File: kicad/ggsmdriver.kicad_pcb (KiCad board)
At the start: 4 copper layers, 55 x 45 mm, 69 parts, among them J1 DC-005, J2 VIN 9-24V, J3 MOTOR A1 A2 B1 B2, J4 EXP, J5 USB-C, SW1 BOOT, SW2 RESET, U1 STM32G0B1CBT6, U2 TMC2209-LA, U3 TPS54202DDCR, U4 XC6206P332MR, U5 USBLC6-2SC6

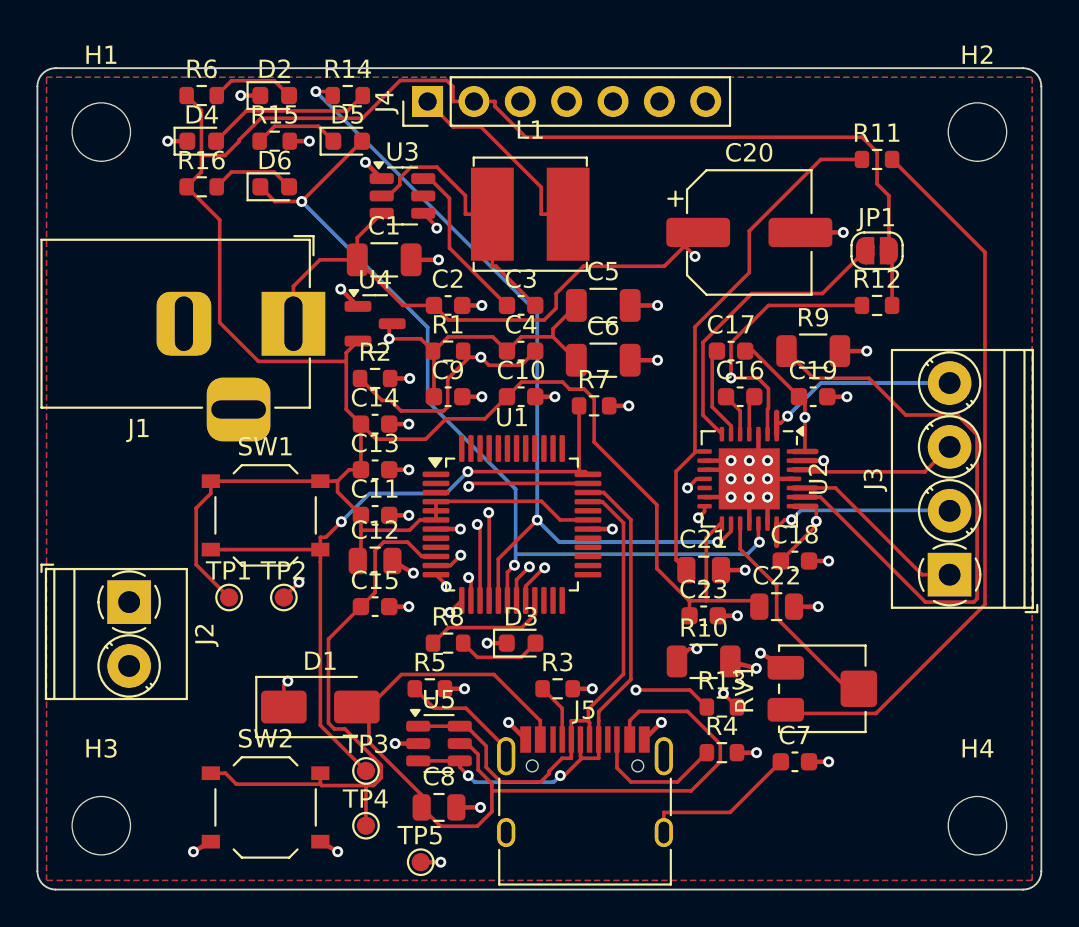
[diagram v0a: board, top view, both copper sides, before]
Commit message: PCB: hand-laid TMC2209 power stage, no VREF trimmer, real track widths
Motor outputs run 1 mm wide straight to J3 next to the chip (J3 now A2 A1 B1 B2),
sense resistors and VS vias sit at the driver pins, VS caps join through a new
In2.Cu VIN plane, as on the Adafruit breakout. VREF goes to GND since current is
always set over UART. Netclass widths now reach the router. Fully routed, no DRC
errors; fab files regenerated.

Co-Authored-By: Claude Opus 5.5 (1M context) <noreply@anthropic.com>
Claude-Session: https://claude.ai/code/session_01VFhb1Qv7mkaGrgvtw2CS4q
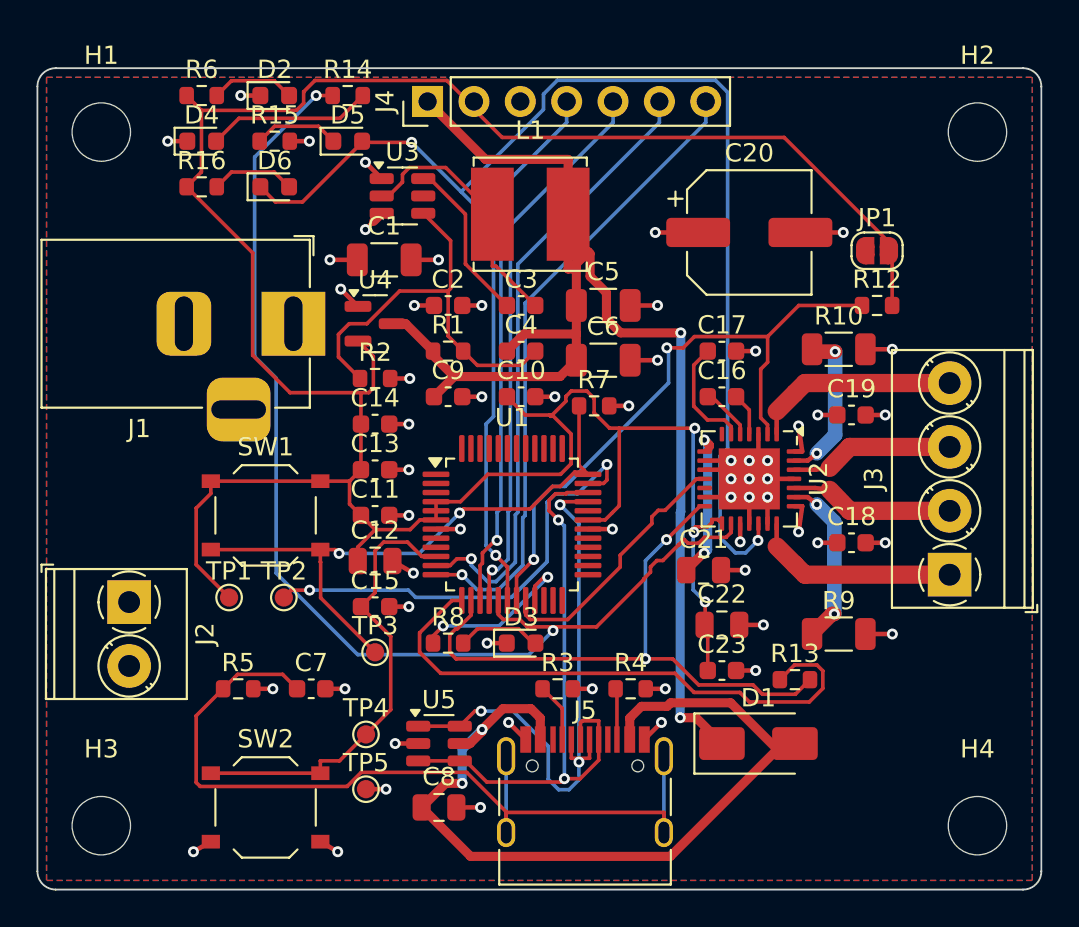
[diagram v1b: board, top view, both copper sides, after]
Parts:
- removed R11: 33k, Resistor_SMD:R_0603_1608Metric
- removed RV1: 10k current, Potentiometer_SMD:Potentiometer_Bourns_3314J_Vertical
- J3: value MOTOR A1 A2 B1 B2 -> MOTOR A2 A1 B1 B2
- moved C7 26.8 mm to (115.0, 134.0)
- moved D1 24.1 mm to (139.5, 137.0)
- moved R10 18.6 mm to (143.9, 115.4)
- moved R9 15.6 mm to (143.9, 131.0)
- moved R5 10.5 mm to (111.0, 134.0)
- moved TP3 6.52 mm to (118.5, 132.0)
- moved R4 6.10 mm to (132.5, 134.0)
- moved TP4 5.00 mm to (118.0, 136.5)
- moved TP5 5.00 mm to (118.0, 139.5)
- moved R13 4.27 mm to (141.5, 133.5)
- moved C18 3.26 mm to (144.6, 126.0)
- moved C22 3.16 mm to (137.5, 130.5)
- moved C23 3.16 mm to (137.5, 133.0)
- moved C19 2.33 mm to (144.6, 119.0)
- moved C16 1.00 mm to (137.5, 118.0)
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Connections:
- J3 pad 1: MOT_A1 -> MOT_A2
- J3 pad 2: MOT_A2 -> MOT_A1
- U2 pad 17: TMC_VREF -> GND
- U2 pad 7: TMC_SPREAD -> (no net)
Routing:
- net VIN: track 83.2 -> 13.8 mm, vias 3 -> 9
- net TMC_POT: track 40.0 -> 0.00 mm
- net TMC_DIR: track 48.8 -> 83.8 mm
- net TMC_BRA: track 33.8 -> 9.46 mm, vias 0 -> 2
- net TMC_5V: track 28.8 -> 8.59 mm, vias 0 -> 2
- net TMC_STEP: track 46.6 -> 63.5 mm, vias 3 -> 2
- net TMC_SPREAD: track 16.4 -> 0.00 mm
- net USB_SHIELD: track 32.4 -> 48.0 mm
- net TMC_TX: track 17.2 -> 31.4 mm, vias 2 -> 0
- net TMC_VREF: track 12.1 -> 0.00 mm
- net TMC_UART: track 25.4 -> 34.2 mm, vias 3 -> 2
- net TMC_BRB: track 16.2 -> 8.70 mm
- net BOOT0_SWCLK: track 39.7 -> 33.2 mm
- net +5V: track 65.2 -> 71.7 mm
- net NRST: track 31.5 -> 25.3 mm
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- added copper zone on In2.Cu, net VIN

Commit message: PCB round 2: no barrel jack, power terminal beside motor terminal, stocked parts
J1 removed; the VIN/GND terminal sits right below the motor terminal on the right
edge. TMC2209-LA-T (C2150710), RALEC 50 mOhm 1206 sense resistors (C154645), red
Basic / green LEDs replace out-of-stock parts. SPREAD pin reconnected (lost in the
previous edit). Fully routed, no DRC errors; fab files regenerated.

Co-Authored-By: Claude Opus 5.5 (1M context) <noreply@anthropic.com>
Claude-Session: https://claude.ai/code/session_01VFhb1Qv7mkaGrgvtw2CS4q
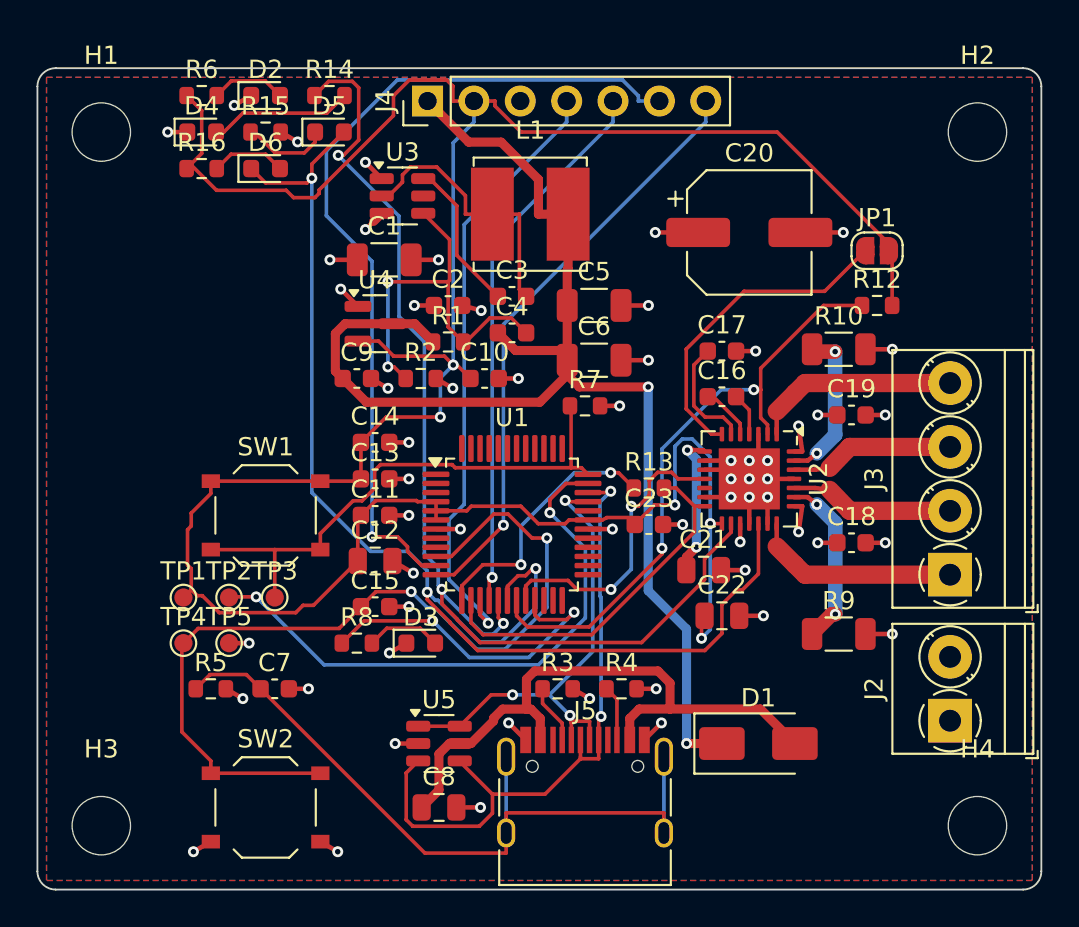
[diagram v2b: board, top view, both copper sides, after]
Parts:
- removed J1: DC-005, Connector_BarrelJack:BarrelJack_Horizontal
- D2: value PWR green -> PWR red
- D3: value STATUS blue -> STATUS green
- D4: value STEP yellow -> STEP red
- J2: value VIN 9-24V -> VIN 9-24V GND
- U2: value TMC2209-LA -> TMC2209-LA-T
- moved J2 45.4 mm to (150.0, 135.8), turned to 90 degrees
- moved R13 13.2 mm to (133.5, 123.0)
- moved TP4 11.2 mm to (108.0, 131.5)
- moved TP5 11.0 mm to (110.5, 131.5)
- moved C23 8.94 mm to (133.5, 125.0)
- moved TP3 6.26 mm to (113.0, 129.0)
- moved D3 5.50 mm to (121.0, 131.5)
- moved C9 5.10 mm to (117.5, 117.0)
- moved R8 5.00 mm to (117.5, 131.5)
- moved TP2 3.00 mm to (110.5, 129.0)
- moved R2 2.50 mm to (121.0, 117.0)
- moved TP1 2.50 mm to (108.0, 129.0)
- moved C10 2.24 mm to (124.5, 117.0)
- moved C7 2.00 mm to (113.0, 134.0)
- moved R5 1.50 mm to (109.5, 134.0)
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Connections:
- U2 pad 7: (no net) -> TMC_SPREAD
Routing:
- net NRST: track 25.3 -> 48.5 mm, vias 0 -> 2
- net TMC_SPREAD: track 0.00 -> 17.8 mm
- net TMC_TX: track 31.4 -> 14.4 mm, vias 0 -> 2
- net TMC_UART: track 34.2 -> 20.1 mm, vias 2 -> 0
- net VBUS: track 47.6 -> 34.0 mm, vias 2 -> 0
- net ENC_A: track 34.2 -> 47.0 mm
- net TMC_DIR: track 83.8 -> 71.4 mm
- net LED_STAT_R: track 9.71 -> 18.3 mm
- net SWDIO: track 24.9 -> 31.9 mm
- net USB_SHIELD: track 48.0 -> 41.7 mm
- net USB_DM: track 32.6 -> 26.4 mm
- net IO1: track 29.4 -> 33.6 mm
- net USB_DP: track 32.9 -> 36.2 mm
- net BOOT0_SWCLK: track 33.2 -> 29.9 mm, vias 2 -> 0
- net +3V3: track 149.8 -> 153.0 mm, vias 3 -> 5
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
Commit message: PCB: stocked 22 uF cap and three 2-pole terminals
C20 is now Lelon VES220M1HTR-0605 (C176676). The out-of-stock 4-pole motor terminal is
split into two KF350-3.5-2P blocks (J6 coil B, J3 coil A), so power and motor are three
identical 2P blocks along the right edge. Coil B tracks, R10 and C19 moved to make room.
Fully routed, no DRC errors; fab files regenerated.

Co-Authored-By: Claude Opus 5.5 (1M context) <noreply@anthropic.com>
Claude-Session: https://claude.ai/code/session_01VFhb1Qv7mkaGrgvtw2CS4q
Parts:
- added J6: MOTOR B1 B2, TerminalBlock_Phoenix:TerminalBlock_Phoenix_PT-1,5-2-3.5-H_1x02_P3.50mm_Horizontal, F.Cu at (150.0, 119.5)
- C20: footprint Capacitor_SMD:CP_Elec_6.3x5.9 -> Capacitor_SMD:CP_Elec_6.3x5.4
- J3: value MOTOR A2 A1 B1 B2 -> MOTOR A2 A1; footprint TerminalBlock_Phoenix:TerminalBlock_Phoenix_PT-1,5-4-3.5-H_1x04_P3.50mm_Horizontal -> TerminalBlock_Phoenix:TerminalBlock_Phoenix_PT-1,5-2-3.5-H_1x02_P3.50mm_Horizontal
- moved R10 2.48 mm to (142.0, 113.8)
- moved C19 1.25 mm to (144.6, 117.8)
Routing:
- net TMC_TX: track 14.4 -> 51.7 mm
- net BOOT0_SWCLK: track 29.9 -> 63.5 mm, vias 0 -> 2
- net TMC_EN: track 34.0 -> 58.7 mm, vias 2 -> 0
- net TMC_UART: track 20.1 -> 42.7 mm, vias 0 -> 2
- net NRST: track 48.5 -> 32.0 mm, vias 2 -> 0
- net USB_DM: track 26.4 -> 40.9 mm, vias 3 -> 2
- net ENC_A: track 47.0 -> 34.8 mm
- net TMC_DIR: track 71.4 -> 59.8 mm, vias 3 -> 4
- net SWDIO: track 31.9 -> 23.7 mm, vias 2 -> 0
- net +3V3: track 153.0 -> 144.9 mm
- net TMC_STEP: track 60.7 -> 68.2 mm, vias 3 -> 4
- net BUCK_FB: track 21.5 -> 15.9 mm, vias 2 -> 0
- net IO1: track 33.6 -> 36.7 mm
- net LED_STAT_R: track 18.3 -> 16.2 mm
- net TMC_BRB: track 8.70 -> 10.1 mm
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
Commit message: PCB: one 6-pole 2.54 mm terminal for power and motor
KF128-2.54-6P (C474924) replaces the three 3.5 mm 2-pole blocks, as on the Adafruit
breakout. Motor tracks re-laid to the 2.54 mm pins. Fully routed, no DRC errors; fab files
regenerated.

Co-Authored-By: Claude Opus 5.5 (1M context) <noreply@anthropic.com>
Claude-Session: https://claude.ai/code/session_01VFhb1Qv7mkaGrgvtw2CS4q
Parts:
- removed J2: VIN 9-24V GND, TerminalBlock_Phoenix:TerminalBlock_Phoenix_PT-1,5-2-3.5-H_1x02_P3.50mm_Horizontal
- removed J6: MOTOR B1 B2, TerminalBlock_Phoenix:TerminalBlock_Phoenix_PT-1,5-2-3.5-H_1x02_P3.50mm_Horizontal
- J3: value MOTOR A2 A1 -> VIN GND A2 A1 B1 B2; footprint TerminalBlock_Phoenix:TerminalBlock_Phoenix_PT-1,5-2-3.5-H_1x02_P3.50mm_Horizontal -> TerminalBlock_Phoenix:TerminalBlock_Phoenix_MPT-0,5-6-2.54_1x06_P2.54mm_Horizontal
- moved J3 3.90 mm to (151.4, 131.4)
- moved C18 2.40 mm to (144.6, 128.4)
- moved C19 1.15 mm to (144.6, 116.6)
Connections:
- J3 pad 1: MOT_A2 -> VIN
- J3 pad 2: MOT_A1 -> GND
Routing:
- net TMC_TX: track 51.7 -> 18.2 mm
- net BOOT0_SWCLK: track 63.5 -> 32.2 mm, vias 2 -> 0
- net SWDIO: track 23.7 -> 53.1 mm, vias 0 -> 2
- net TMC_UART: track 42.7 -> 21.8 mm
- net TMC_EN: track 58.7 -> 38.9 mm, vias 0 -> 2
- net VBUS: track 34.1 -> 53.4 mm
- net LED_STAT_R: track 16.2 -> 30.6 mm
- net USB_DM: track 40.9 -> 29.1 mm
- net +3V3: track 144.9 -> 136.6 mm, vias 5 -> 2
- net USB_DP: track 36.6 -> 44.2 mm
- net +5V: track 73.4 -> 77.2 mm, vias 3 -> 2
- net TMC_STEP: track 68.2 -> 64.7 mm, vias 4 -> 3
- net TMC_DIAG: track 16.4 -> 19.7 mm, vias 0 -> 2
- net TMC_DIR: track 59.8 -> 62.8 mm, vias 4 -> 3
- net IO1: track 36.7 -> 34.0 mm
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
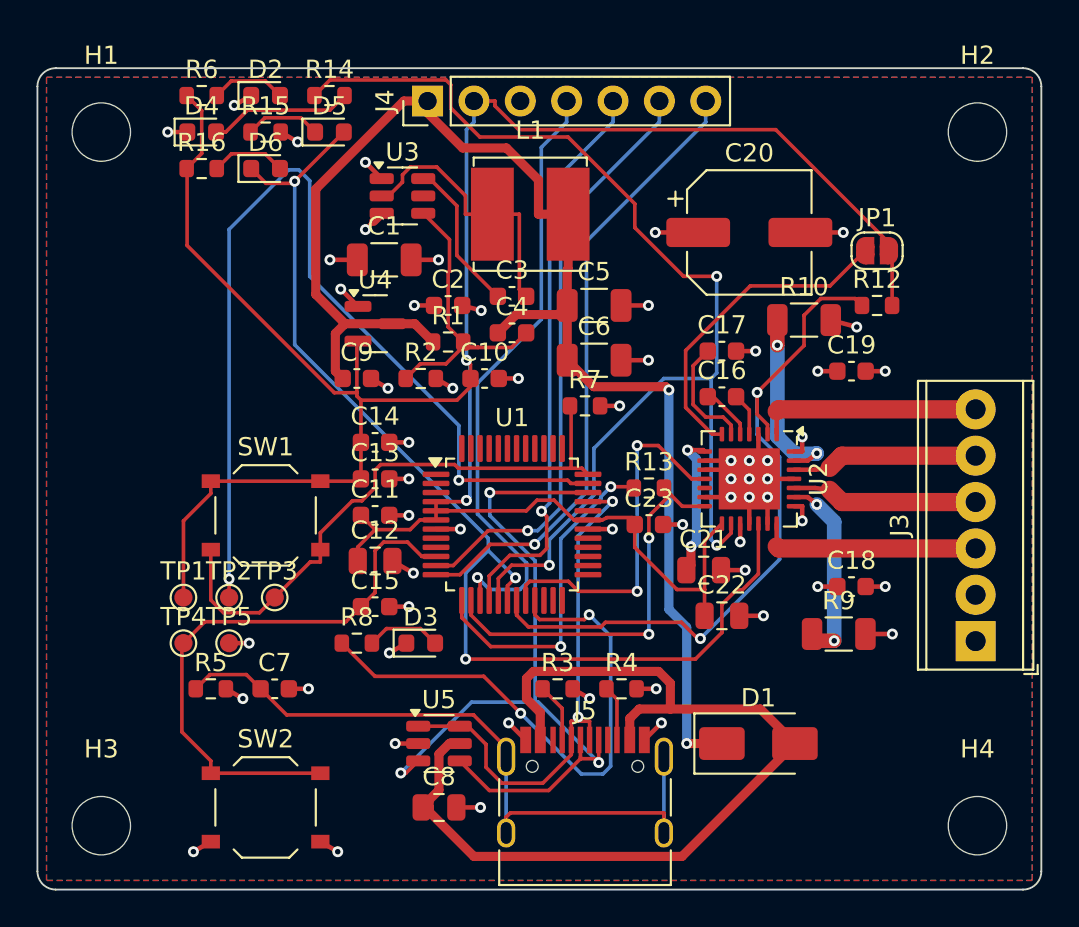
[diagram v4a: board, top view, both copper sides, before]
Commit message: PCB: hand-laid buck switch node and USB D+/D- pair
U3 turned so its SW pin feeds L1 through a short 0.8 mm track. USB D+/D- run as one
0.25/0.15 mm pair on F.Cu over the GND plane (about 90 ohm differential, estimated) through
the USBLC6 flow-through pads, with a DRC rule file allowing the 0.15 mm gap between them.
Fully routed, no DRC errors; fab files regenerated.

Co-Authored-By: Claude Opus 5.5 (1M context) <noreply@anthropic.com>
Claude-Session: https://claude.ai/code/session_01VFhb1Qv7mkaGrgvtw2CS4q
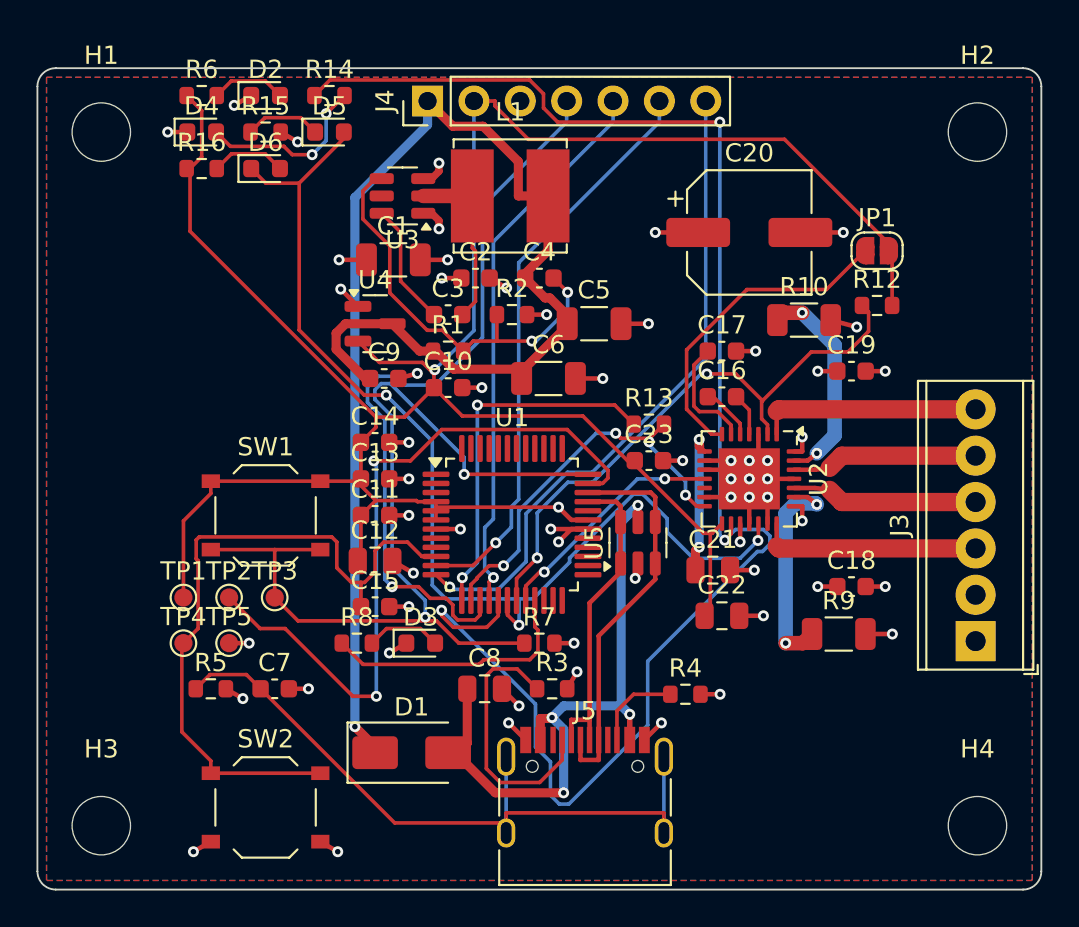
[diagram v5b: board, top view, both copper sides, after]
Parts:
- moved D1 19.0 mm to (120.5, 137.5)
- moved U5 15.5 mm to (132.9, 126.0), turned to 90 degrees
- moved R7 13.2 mm to (127.5, 131.5)
- moved C8 6.96 mm to (124.5, 134.0)
- moved R2 6.10 mm to (126.0, 113.5)
- moved C3 3.64 mm to (122.5, 113.5)
- moved R4 3.51 mm to (135.5, 134.3)
- moved C23 3.50 mm to (133.5, 121.5)
- moved R13 3.50 mm to (133.5, 119.5)
- moved C4 3.35 mm to (127.5, 111.5)
- moved C6 2.69 mm to (128.0, 117.0)
- moved C2 2.12 mm to (124.0, 111.5)
- moved C10 2.06 mm to (122.5, 117.5)
- moved C9 1.50 mm to (119.0, 117.0)
- moved L1 1.49 mm to (125.9, 107.0)
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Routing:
- net TMC_STEP: track 64.7 -> 88.9 mm
- net USB_DP: track 44.2 -> 21.6 mm, vias 3 -> 0
- net BOOT0_SWCLK: track 32.2 -> 51.6 mm, vias 0 -> 2
- net VBUS: track 53.4 -> 35.7 mm, vias 0 -> 4
- net LED_STAT_R: track 30.6 -> 14.4 mm, vias 2 -> 0
- net SWDIO: track 53.1 -> 39.4 mm
- net USB_DM: track 29.1 -> 17.5 mm, vias 2 -> 0
- net USB_CC1: track 3.25 -> 14.6 mm
- net IO1: track 34.0 -> 41.0 mm
- net TMC_DIAG: track 19.7 -> 13.0 mm
- net TMC_EN: track 38.9 -> 32.3 mm
- net NRST: track 31.6 -> 38.2 mm
- net BUCK_FB: track 16.6 -> 23.0 mm, vias 0 -> 2
- net BUCK_SW: track 14.7 -> 9.56 mm
- net TMC_DIR: track 62.8 -> 59.5 mm
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
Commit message: Swap Extended passives to JLC Basic, hand-solder the header
C16 -> C21122, C17-19/C23 220nF -> 100nF C14663, C4 75pF -> 100pF C14858.
J4 drops its LCSC number so it stays out of the JLC BOM/CPL. Board
re-routed (0 unrouted, no DRC errors) and fab files regenerated.

Co-Authored-By: Claude Opus 5.5 (1M context) <noreply@anthropic.com>
Claude-Session: https://claude.ai/code/session_01VFhb1Qv7mkaGrgvtw2CS4q
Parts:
- C17, C18, C19: value 220nF 50V -> 100nF 50V
- C23: value 220nF -> 100nF
- C4: value 75pF -> 100pF
- D3: value STATUS green -> STATUS red
- D5: value DIR red -> DIR+ red
- D6: value DIR green -> DIR- red
